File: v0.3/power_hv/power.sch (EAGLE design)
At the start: 55 parts, among them IC1 ACS758ECB-200B-PFF-T, IC3 ACS758ECB-200B-PFF-T, Q1 FDB86135, Q10 FDB86135, Q11 FDB86135, Q12 FDB86135, Q2 FDB86135, Q3 FDB86135, Q4 FDB86135, Q5 FDB86135, Q6 FDB86135, Q7 FDB86135, Q8 FDB86135, Q9 FDB86135

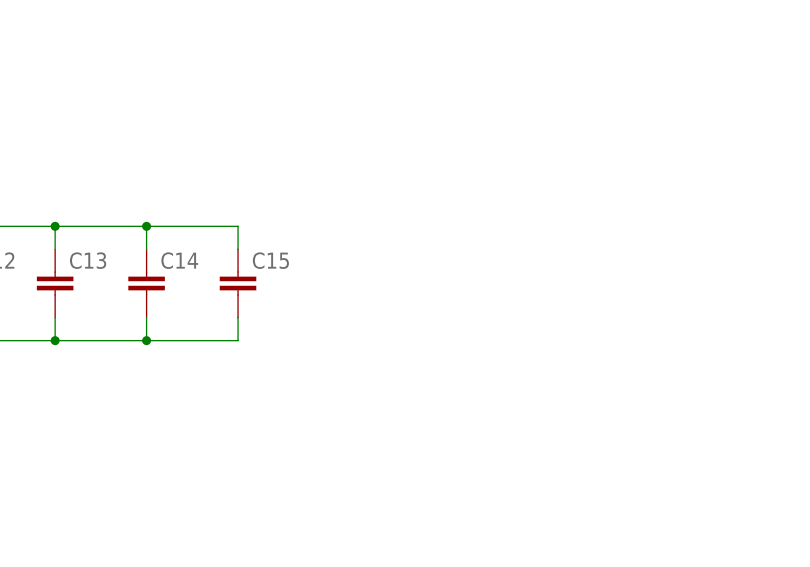
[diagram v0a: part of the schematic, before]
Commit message: TODO: Route ground connection to driver board.
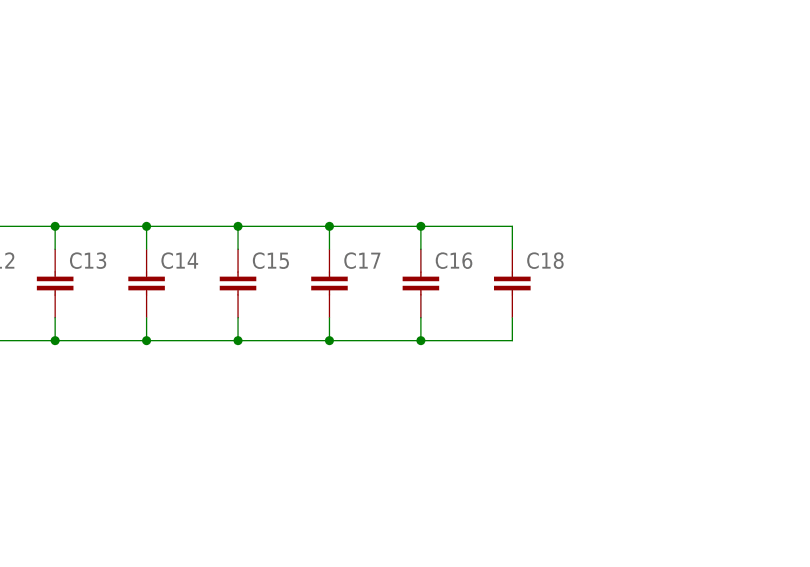
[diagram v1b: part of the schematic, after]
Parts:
- added C16, C17, C18: (no value), rcl:C-EUC2220K
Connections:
- net GND: now also C16.2, C17.2, C18.2
- net VCC: now also C16.1, C17.1, C18.1
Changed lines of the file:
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@@
 <grid distance="0.1" unitdist="inch" unit="inch" style="lines" multiple="1" display="no" altdistance="0.01" altunitdist="inch" altunit="inch"/>
 <layers>
-<layer number="1" name="Top" color="4" fill="1" visible="yes" active="no"/>
-<layer number="2" name="Route2" color="1" fill="3" visible="yes" active="no"/>
-<layer number="3" name="Route3" color="4" fill="3" visible="yes" active="no"/>
-<layer number="4" name="Route4" color="1" fill="4" visible="yes" active="no"/>
-<layer number="5" name="Route5" color="4" fill="4" visible="yes" active="no"/>
-<layer number="6" name="Route6" color="1" fill="8" visible="yes" active="no"/>
-<layer number="7" name="Route7" color="4" fill="8" visible="yes" active="no"/>
-<layer number="8" name="Route8" color="1" fill="2" visible="yes" active="no"/>
-<layer number="9" name="Route9" color="4" fill="2" visible="yes" active="no"/>
-<layer number="10" name="Route10" color="1" fill="7" visible="yes" active="no"/>
-<layer number="11" name="Route11" color="4" fill="7" visible="yes" active="no"/>
-<layer number="12" name="Route12" color="1" fill="5" visible="yes" active="no"/>
-<layer number="13" name="Route13" color="4" fill="5" visible="yes" active="no"/>
-<layer number="14" name="Route14" color="1" fill="6" visible="yes" active="no"/>
-<layer number="15" name="Route15" color="4" fill="6" visible="yes" active="no"/>
-<layer number="16" name="Bottom" color="1" fill="1" visible="yes" active="no"/>
-<layer number="17" name="Pads" color="2" fill="1" visible="yes" active="no"/>
-<layer number="18" name="Vias" color="2" fill="1" visible="yes" active="no"/>
-<layer number="19" name="Unrouted" color="6" fill="1" visible="yes" active="no"/>
-<layer number="20" name="Dimension" color="15" fill="1" visible="yes" active="no"/>
-<layer number="21" name="tPlace" color="7" fill="1" visible="yes" active="no"/>
-<layer number="22" name="bPlace" color="7" fill="1" visible="yes" active="no"/>
-<layer number="23" name="tOrigins" color="15" fill="1" visible="yes" active="no"/>
-<layer number="24" name="bOrigins" color="15" fill="1" visible="yes" active="no"/>
-<layer number="25" name="tNames" color="7" fill="1" visible="yes" active="no"/>
-<layer number="26" name="bNames" color="7" fill="1" visible="yes" active="no"/>
-<layer number="27" name="tValues" color="7" fill="1" visible="yes" active="no"/>
-<layer number="28" name="bValues" color="7" fill="1" visible="yes" active="no"/>
+<layer number="1" name="Top" color="4" fill="1" visible="no" active="no"/>
+<layer number="2" name="Route2" color="1" fill="3" visible="no" active="no"/>
+<layer number="3" name="Route3" color="4" fill="3" visible="no" active="no"/>
+<layer number="4" name="Route4" color="1" fill="4" visible="no" active="no"/>
+<layer number="5" name="Route5" color="4" fill="4" visible="no" active="no"/>
+<layer number="6" name="Route6" color="1" fill="8" visible="no" active="no"/>
+<layer number="7" name="Route7" color="4" fill="8" visible="no" active="no"/>
+<layer number="8" name="Route8" color="1" fill="2" visible="no" active="no"/>
+<layer number="9" name="Route9" color="4" fill="2" visible="no" active="no"/>
+<layer number="10" name="Route10" color="1" fill="7" visible="no" active="no"/>
+<layer number="11" name="Route11" color="4" fill="7" visible="no" active="no"/>
+<layer number="12" name="Route12" color="1" fill="5" visible="no" active="no"/>
+<layer number="13" name="Route13" color="4" fill="5" visible="no" active="no"/>
+<layer number="14" name="Route14" color="1" fill="6" visible="no" active="no"/>
+<layer number="15" name="Route15" color="4" fill="6" visible="no" active="no"/>
+<layer number="16" name="Bottom" color="1" fill="1" visible="no" active="no"/>
+<layer number="17" name="Pads" color="2" fill="1" visible="no" active="no"/>
+<layer number="18" name="Vias" color="2" fill="1" visible="no" active="no"/>
+<layer number="19" name="Unrouted" color="6" fill="1" visible="no" active="no"/>
+<layer number="20" name="Dimension" color="15" fill="1" visible="no" active="no"/>
+<layer number="21" name="tPlace" color="7" fill="1" visible="no" active="no"/>
+<layer number="22" name="bPlace" color="7" fill="1" visible="no" active="no"/>
+<layer number="23" name="tOrigins" color="15" fill="1" visible="no" active="no"/>
+<layer number="24" name="bOrigins" color="15" fill="1" visible="no" active="no"/>
+<layer number="25" name="tNames" color="7" fill="1" visible="no" active="no"/>
+<layer number="26" name="bNames" color="7" fill="1" visible="no" active="no"/>
+<layer number="27" name="tValues" color="7" fill="1" visible="no" active="no"/>
+<layer number="28" name="bValues" color="7" fill="1" visible="no" active="no"/>
 <layer number="29" name="tStop" color="7" fill="3" visible="no" active="no"/>
 <layer number="30" name="bStop" color="7" fill="6" visible="no" active="no"/>
@@
 <layer number="35" name="tGlue" color="7" fill="4" visible="no" active="no"/>
 <layer number="36" name="bGlue" color="7" fill="5" visible="no" active="no"/>
-<layer number="37" name="tTest" color="7" fill="1" visible="yes" active="no"/>
-<layer number="38" name="bTest" color="7" fill="1" visible="yes" active="no"/>
+<layer number="37" name="tTest" color="7" fill="1" visible="no" active="no"/>
+<layer number="38" name="bTest" color="7" fill="1" visible="no" active="no"/>
 <layer number="39" name="tKeepout" color="4" fill="11" visible="no" active="no"/>
 <layer number="40" name="bKeepout" color="1" fill="11" visible="no" active="no"/>
@@
 <layer number="44" name="Drills" color="7" fill="1" visible="no" active="no"/>
 <layer number="45" name="Holes" color="7" fill="1" visible="no" active="no"/>
-<layer number="46" name="Milling" color="3" fill="1" visible="yes" active="no"/>
-<layer number="47" name="Measures" color="7" fill="1" visible="yes" active="no"/>
-<layer number="48" name="Document" color="7" fill="1" visible="yes" active="no"/>
-<layer number="49" name="Reference" color="7" fill="1" visible="yes" active="no"/>
-<layer number="50" name="dxf" color="7" fill="1" visible="yes" active="no"/>
-<layer number="51" name="tDocu" color="7" fill="1" visible="yes" active="no"/>
-<layer number="52" name="bDocu" color="7" fill="1" visible="yes" active="no"/>
-<layer number="53" name="tGND_GNDA" color="7" fill="9" visible="yes" active="no"/>
-<layer number="54" name="bGND_GNDA" color="1" fill="9" visible="yes" active="no"/>
-<layer number="56" name="wert" color="7" fill="1" visible="yes" active="no"/>
+<layer number="46" name="Milling" color="3" fill="1" visible="no" active="no"/>
+<layer number="47" name="Measures" color="7" fill="1" visible="no" active="no"/>
+<layer number="48" name="Document" color="7" fill="1" visible="no" active="no"/>
+<layer number="49" name="Reference" color="7" fill="1" visible="no" active="no"/>
+<layer number="50" name="dxf" color="7" fill="1" visible="no" active="no"/>
+<layer number="51" name="tDocu" color="7" fill="1" visible="no" active="no"/>
+<layer number="52" name="bDocu" color="7" fill="1" visible="no" active="no"/>
+<layer number="53" name="tGND_GNDA" color="7" fill="9" visible="no" active="no"/>
+<layer number="54" name="bGND_GNDA" color="1" fill="9" visible="no" active="no"/>
+<layer number="56" name="wert" color="7" fill="1" visible="no" active="no"/>
 <layer number="91" name="Nets" color="2" fill="1" visible="yes" active="yes"/>
 <layer number="92" name="Busses" color="1" fill="1" visible="yes" active="yes"/>
@@
 <part name="C15" library="rcl" deviceset="C-EU" device="C2220K"/>
 <part name="C1" library="open-bldc" deviceset="CAPACITOR_AVX_FFB5" device=""/>
+<part name="C17" library="rcl" deviceset="C-EU" device="C2220K"/>
+<part name="C16" library="rcl" deviceset="C-EU" device="C2220K"/>
+<part name="C18" library="rcl" deviceset="C-EU" device="C2220K"/>
 </parts>
 <sheets>
@@
 <instance part="C15" gate="G$1" x="99.06" y="45.72"/>
 <instance part="C1" gate="G$1" x="25.4" y="45.72"/>
+<instance part="C17" gate="G$1" x="109.22" y="45.72"/>
+<instance part="C16" gate="G$1" x="119.38" y="45.72"/>
+<instance part="C18" gate="G$1" x="129.54" y="45.72"/>
 </instances>
 <busses>
@@
 <junction x="25.4" y="50.8"/>
 <pinref part="C1" gate="G$1" pin="1"/>
+<pinref part="C17" gate="G$1" pin="1"/>
+<wire x1="99.06" y1="50.8" x2="109.22" y2="50.8" width="0.1524" layer="91"/>
+<wire x1="109.22" y1="48.26" x2="109.22" y2="50.8" width="0.1524" layer="91"/>
+<pinref part="C16" gate="G$1" pin="1"/>
+<wire x1="109.22" y1="50.8" x2="119.38" y2="50.8" width="0.1524" layer="91"/>
+<wire x1="119.38" y1="50.8" x2="119.38" y2="48.26" width="0.1524" layer="91"/>
+<junction x="99.06" y="50.8"/>
+<junction x="109.22" y="50.8"/>
+<pinref part="C18" gate="G$1" pin="1"/>
+<wire x1="129.54" y1="48.26" x2="129.54" y2="50.8" width="0.1524" layer="91"/>
+<wire x1="129.54" y1="50.8" x2="119.38" y2="50.8" width="0.1524" layer="91"/>
+<junction x="119.38" y="50.8"/>
 </segment>
 <segment>
@@
 <junction x="25.4" y="38.1"/>
 <pinref part="C1" gate="G$1" pin="2"/>
-</segment>
-<segment>
+<pinref part="C17" gate="G$1" pin="2"/>
+<wire x1="99.06" y1="38.1" x2="109.22" y2="38.1" width="0.1524" layer="91"/>
+<wire x1="109.22" y1="38.1" x2="109.22" y2="40.64" width="0.1524" layer="91"/>
+<pinref part="C16" gate="G$1" pin="2"/>
+<wire x1="119.38" y1="40.64" x2="119.38" y2="38.1" width="0.1524" layer="91"/>
+<wire x1="119.38" y1="38.1" x2="109.22" y2="38.1" width="0.1524" layer="91"/>
+<junction x="109.22" y="38.1"/>
+<junction x="99.06" y="38.1"/>
+<pinref part="C18" gate="G$1" pin="2"/>
+<wire x1="129.54" y1="40.64" x2="129.54" y2="38.1" width="0.1524" layer="91"/>
+<wire x1="129.54" y1="38.1" x2="119.38" y2="38.1" width="0.1524" layer="91"/>
+<junction x="119.38" y="38.1"/>
+</segment>
+<segment>
